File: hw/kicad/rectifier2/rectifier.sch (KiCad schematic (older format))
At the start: 84 parts, among them J1 CONN_01X04, J2 SI8621BT-IS, J3 CONN_01X04, J4 CONN_01X01, P1 CONN_01X03, P2 CONN_01X02, P3 CONN_01X02, P4 CONN_01X02, P5 CONN_01X02, P6 CONN_01X02, P7 CONN_01X02, Q1 Q_NPN_BCE, Q2 Q_NMOS_GDS, Q3 Q_NMOS_GDS, U1 ACT4088, U2 STM32F042F6Px, U3 lnk304D, U4 LTV-817, U5 LTV-817, U6 non_plated, U7 non_plated, U8 non_plated

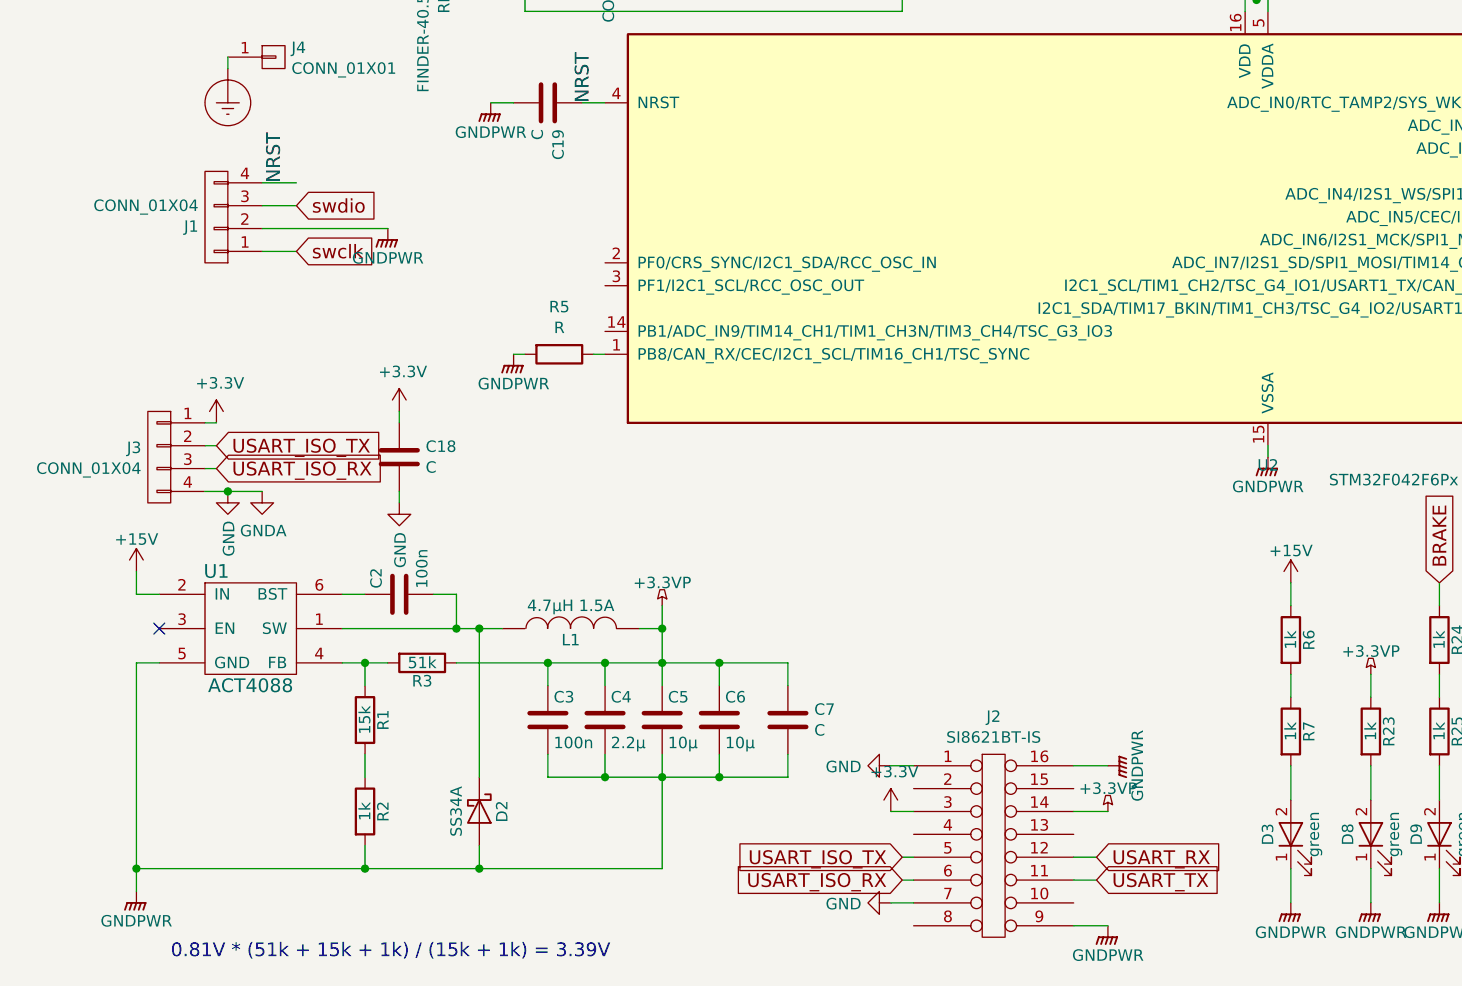
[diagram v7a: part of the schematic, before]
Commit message: Fixed some clearance issues
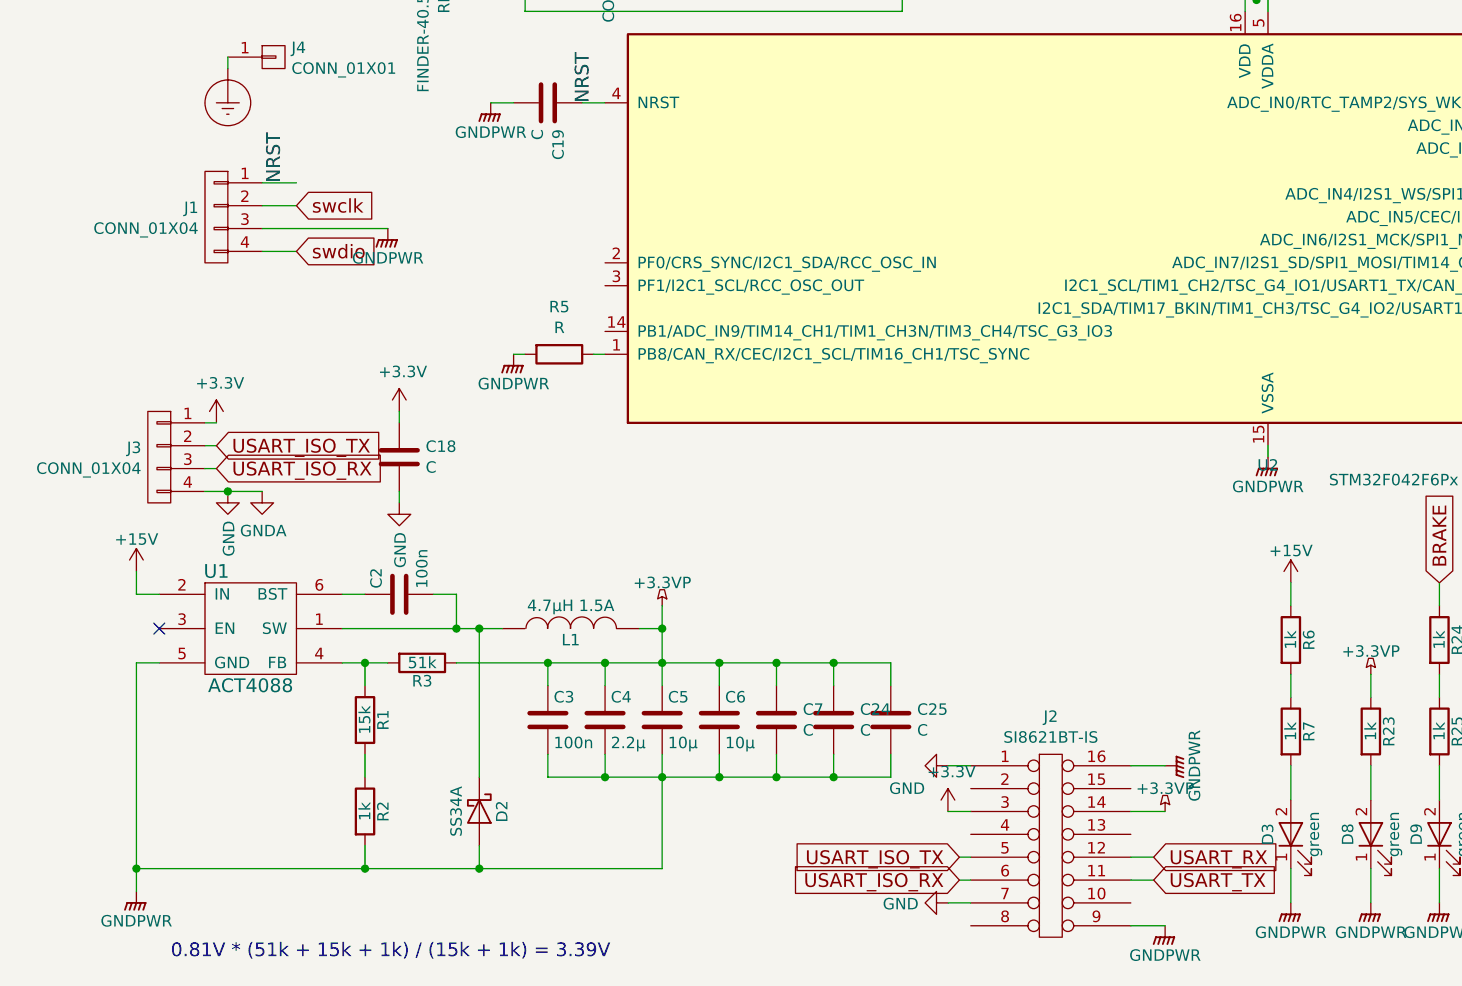
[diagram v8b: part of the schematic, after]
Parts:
- added C24, C25: C, stmbl:C_0603, symbol C
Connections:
- net +3.3VP: now also C24.1, C25.1
- net GNDPWR: now also J1.3 (P3), C24.2, C25.2; no longer J1.2 (P2)
- net NRST: now also J1.1 (P1); no longer J1.4 (P4)
- net swclk: now also J1.2 (P2); no longer J1.1 (P1)
- net swdio: now also J1.4 (P4); no longer J1.3 (P3)
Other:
- moved on the sheet: C7, J2
